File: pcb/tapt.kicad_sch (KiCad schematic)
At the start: 32 parts, among them J1 Conn_01x04_Pin, J2 Conn_01x04_MountingPin, SW1 SW_SPDT_XKB_DMx-xxxx-1, SW2 SW_SPST, U1 nRF52810-QCxx, Y1 32MHz

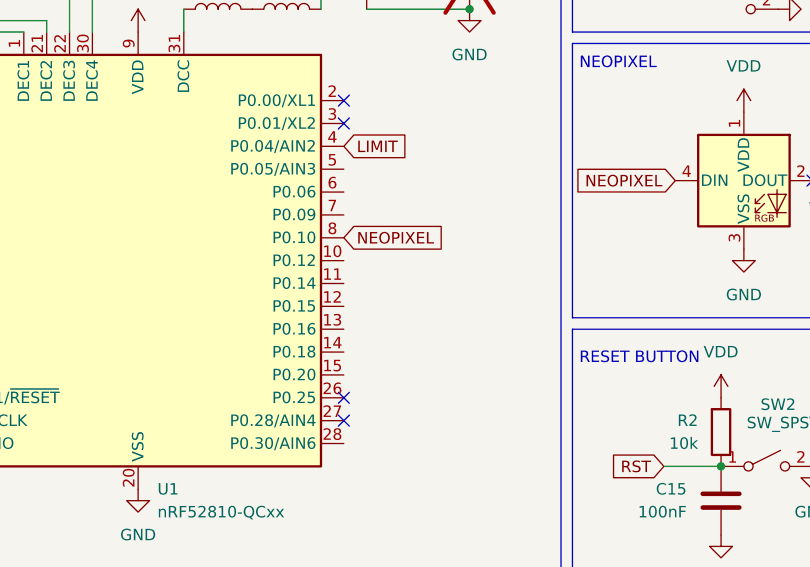
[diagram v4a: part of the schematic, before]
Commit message: pcb: uart, status led
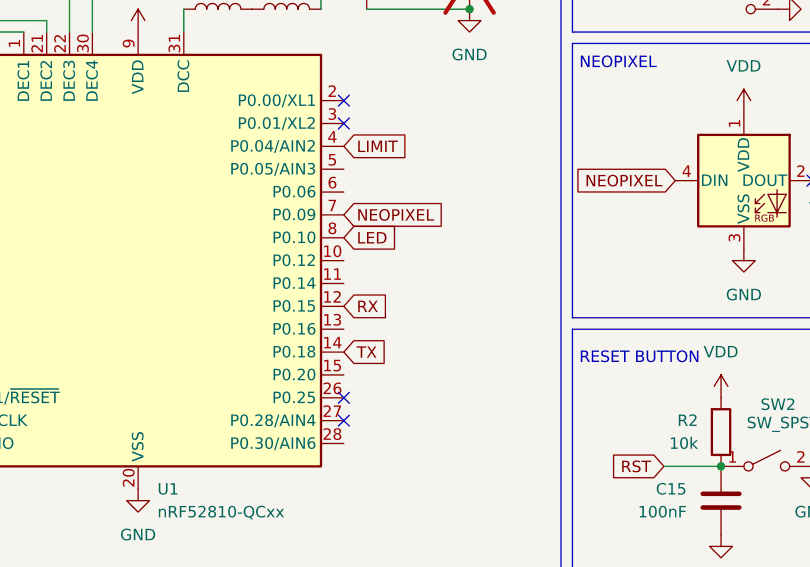
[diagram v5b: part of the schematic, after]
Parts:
- D2: LCSC (none) -> C2297
- J1, J2: now left out of the parts list
- R3: footprint Resistor_SMD:R_0805_2012Metric -> Resistor_SMD:R_0402_1005Metric; LCSC (none) -> C11702
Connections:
- net LED: now also U1.8 (P0.10)
- net NEOPIXEL: now also U1.7 (P0.09); no longer U1.8 (P0.10)
- net RX: now also U1.12 (P0.15)
- net TX: now also U1.14 (P0.18)
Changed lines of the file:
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@@
 		)
 	)
+	(global_label "NEOPIXEL"
+		(shape input)
+		(at 90.17 88.9 0)
+		(fields_autoplaced yes)
+		(effects
+			(font
+				(size 1.27 1.27)
+			)
+			(justify left)
+		)
+		(property "Intersheetrefs" "${INTERSHEET_REFS}"
+			(at 102.2266 88.9 0)
+			(effects
+				(font
+					(size 1.27 1.27)
+				)
+				(justify left)
+				(hide yes)
+			)
+		)
+	)
+	(global_label "RX"
+		(shape input)
+		(at 90.17 99.06 0)
+		(fields_autoplaced yes)
+		(effects
+			(font
+				(size 1.27 1.27)
+			)
+			(justify left)
+		)
+		(property "Intersheetrefs" "${INTERSHEET_REFS}"
+			(at 95.6347 99.06 0)
+			(effects
+				(font
+					(size 1.27 1.27)
+				)
+				(justify left)
+				(hide yes)
+			)
+		)
+	)
 	(global_label "SWDIO"
 		(shape input)
@@
 		)
 	)
+	(global_label "LED"
+		(shape input)
+		(at 90.17 91.44 0)
+		(fields_autoplaced yes)
+		(effects
+			(font
+				(size 1.27 1.27)
+			)
+			(justify left)
+		)
+		(property "Intersheetrefs" "${INTERSHEET_REFS}"
+			(at 96.6023 91.44 0)
+			(effects
+				(font
+					(size 1.27 1.27)
+				)
+				(justify left)
+				(hide yes)
+			)
+		)
+	)
+	(global_label "TX"
+		(shape input)
+		(at 90.17 104.14 0)
+		(fields_autoplaced yes)
+		(effects
+			(font
+				(size 1.27 1.27)
+			)
+			(justify left)
+		)
+		(property "Intersheetrefs" "${INTERSHEET_REFS}"
+			(at 95.3323 104.14 0)
+			(effects
+				(font
+					(size 1.27 1.27)
+				)
+				(justify left)
+				(hide yes)
+			)
+		)
+	)
 	(global_label "SWDCLK"
 		(shape input)
@@
 		)
 	)
-	(global_label "NEOPIXEL"
-		(shape input)
-		(at 90.17 91.44 0)
-		(fields_autoplaced yes)
-		(effects
-			(font
-				(size 1.27 1.27)
-			)
-			(justify left)
-		)
-		(property "Intersheetrefs" "${INTERSHEET_REFS}"
-			(at 102.2266 91.44 0)
-			(effects
-				(font
-					(size 1.27 1.27)
-				)
-				(justify left)
-				(hide yes)
-			)
-		)
-	)
 	(global_label "LED"
 		(shape input)
@@
 			)
 		)
+		(property "LCSC" "C2297"
+			(at 182.88 85.09 0)
+			(effects
+				(font
+					(size 1.27 1.27)
+				)
+				(hide yes)
+			)
+		)
 		(pin "2"
 		)
@@
 			)
 		)
-		(property "Footprint" "Resistor_SMD:R_0805_2012Metric"
+		(property "Footprint" "Resistor_SMD:R_0402_1005Metric"
 			(at 190.5 86.868 90)
 			(effects
@@
 			)
 		)
+		(property "LCSC" "C11702"
+			(at 190.5 85.09 90)
+			(effects
+				(font
+					(size 1.27 1.27)
+				)
+				(hide yes)
+			)
+		)
 		(pin "1"
 		)
@@
 		(unit 1)
 		(exclude_from_sim no)
-		(in_bom yes)
+		(in_bom no)
 		(on_board yes)
 		(dnp no)
@@
 		(unit 1)
 		(exclude_from_sim no)
-		(in_bom yes)
+		(in_bom no)
 		(on_board yes)
 		(dnp no)

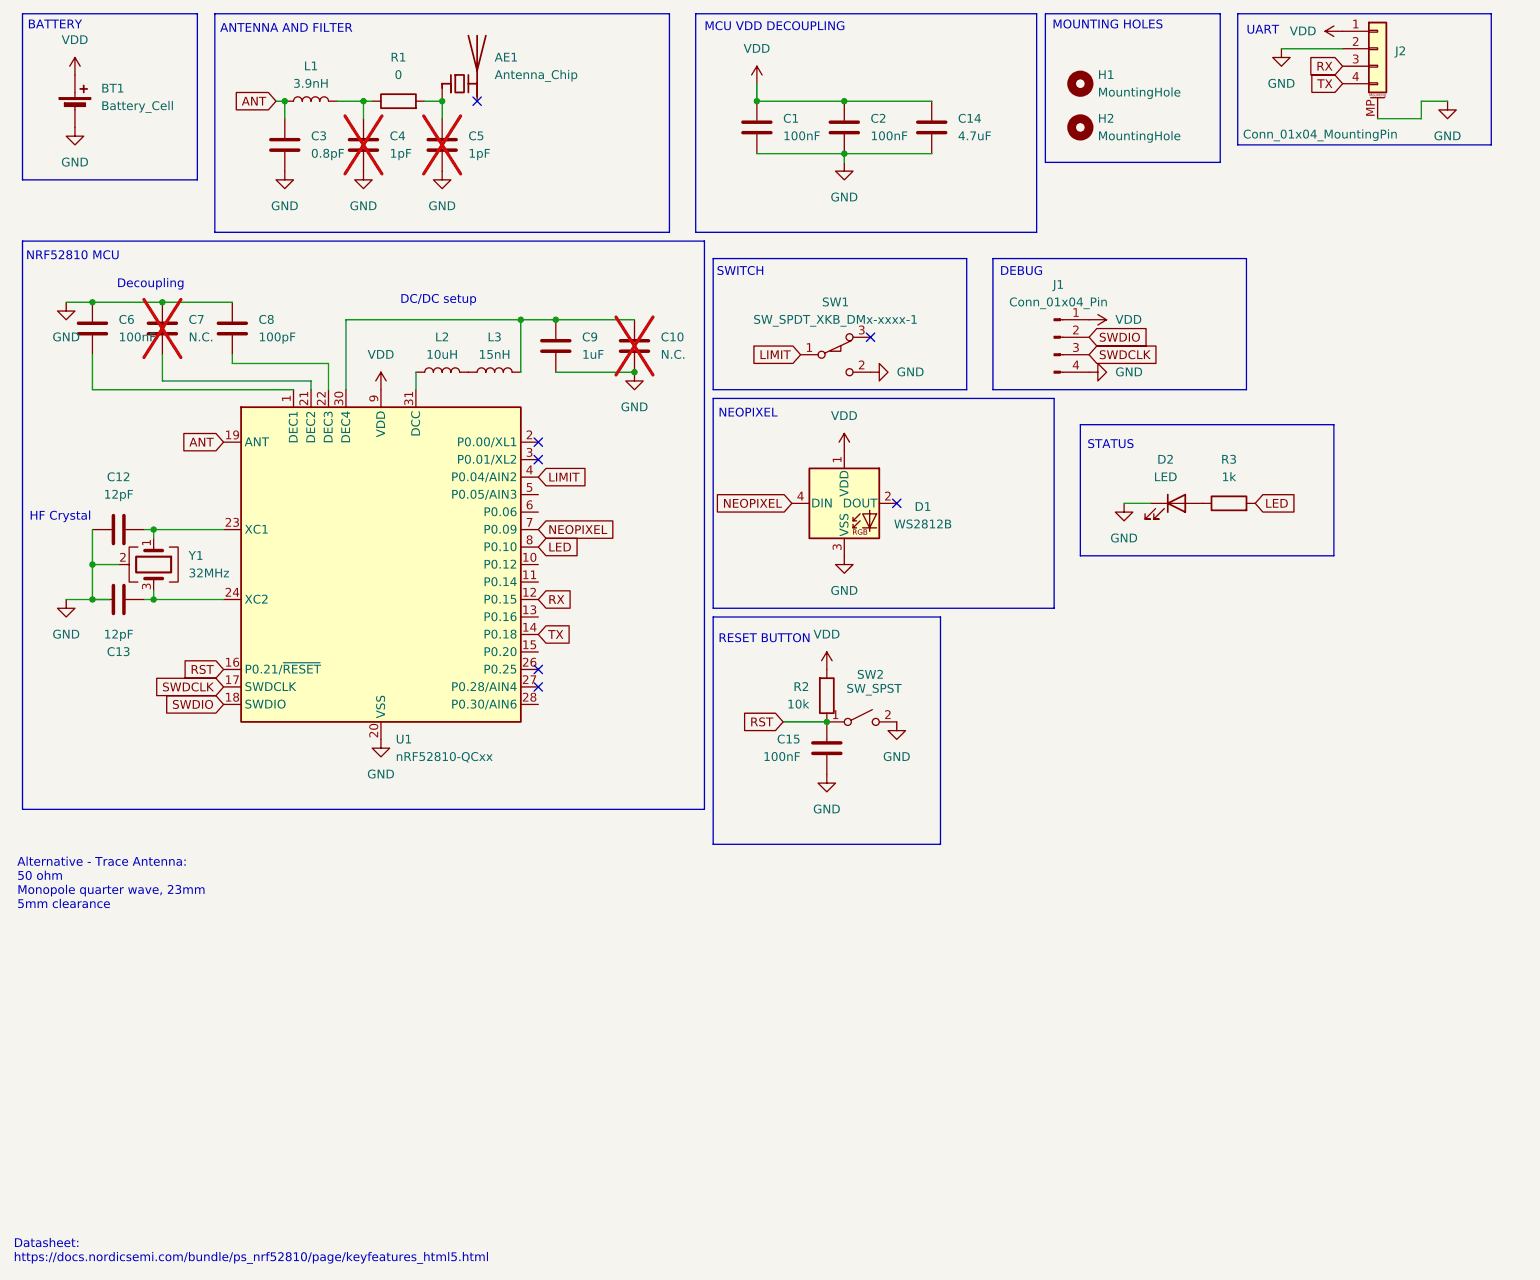
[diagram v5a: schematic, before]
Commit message: pcb: 4 layer redesign, more antenna tuning, low freq crystal
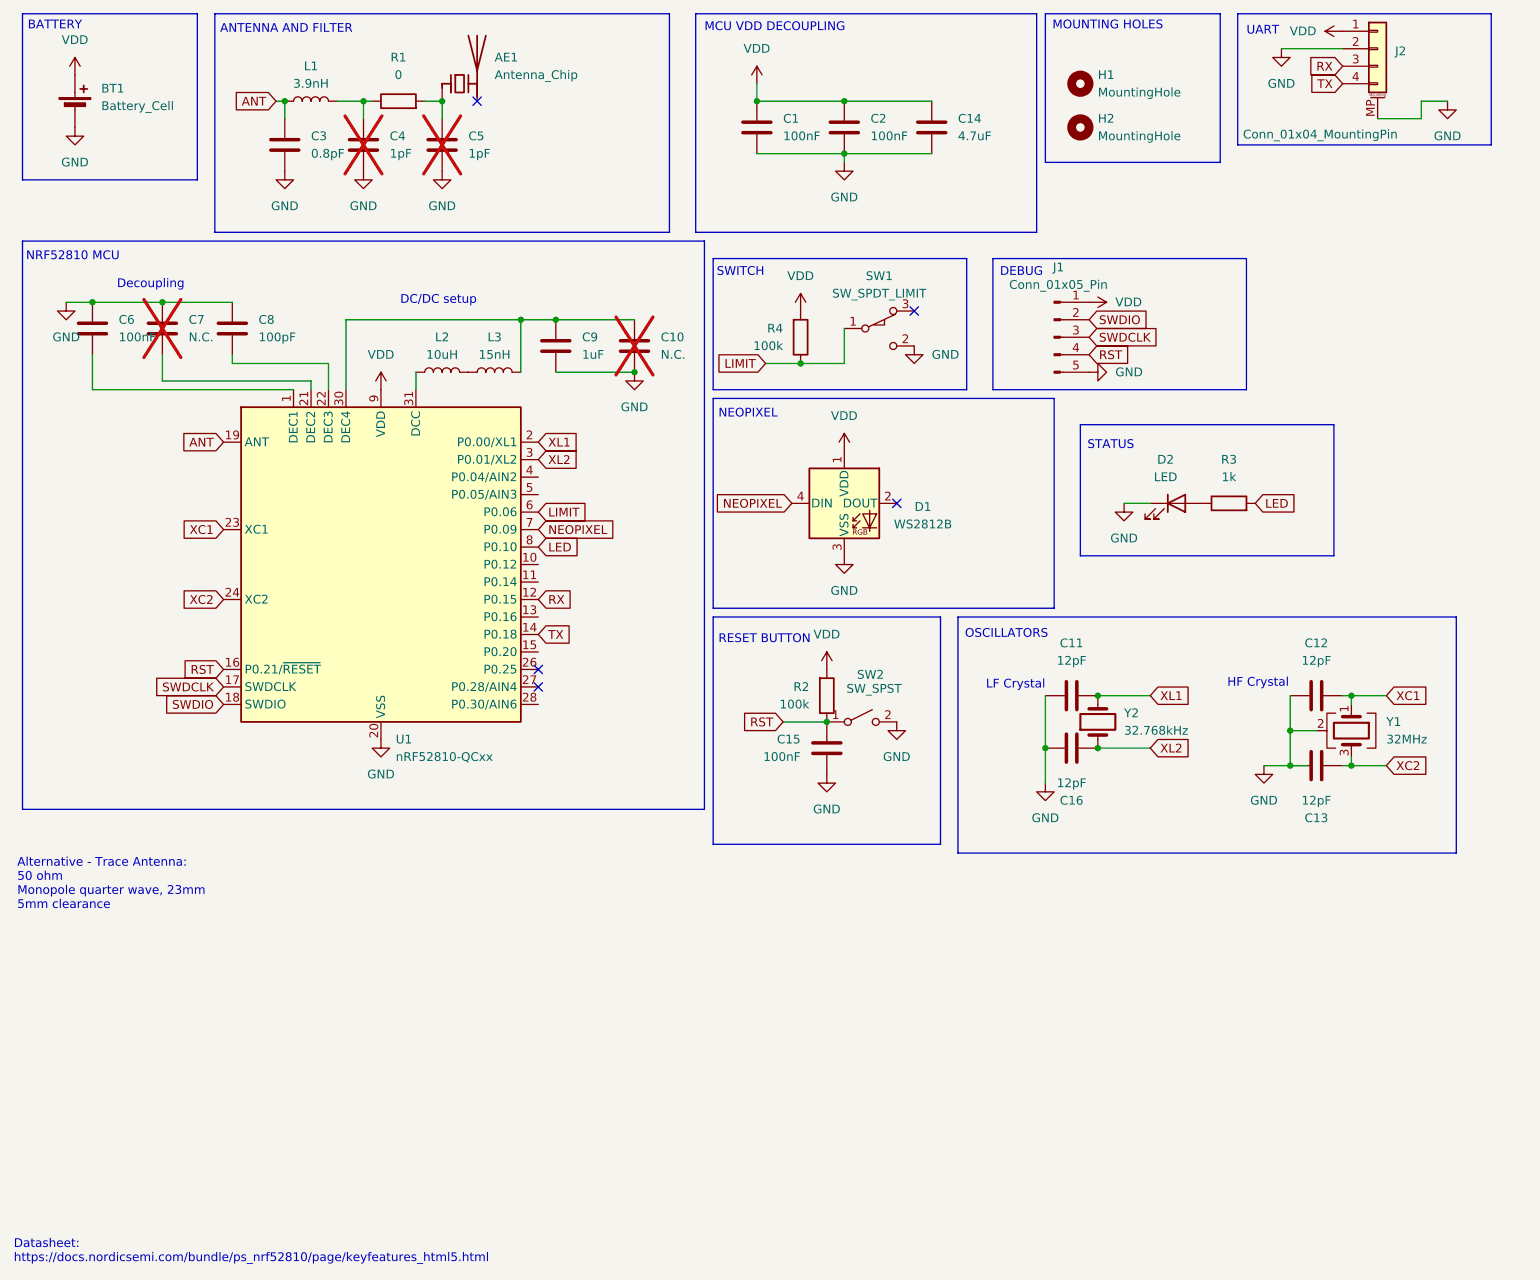
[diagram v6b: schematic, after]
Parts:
- added C11, C16: 12pF, Capacitor_SMD:C_0402_1005Metric, symbol Device:C
- added R4: 100k, Resistor_SMD:R_0402_1005Metric, symbol Device:R
- added Y2: 32.768kHz, Crystal:Crystal_SMD_2012-2Pin_2.0x1.2mm, symbol Device:Crystal
- J1: value Conn_01x04_Pin -> Conn_01x05_Pin; footprint Connector_PinHeader_2.54mm:PinHeader_1x04_P2.54mm_Vertical -> Connector_PinHeader_2.54mm:PinHeader_1x05_P2.54mm_Vertical; symbol Connector:Conn_01x04_Pin -> Connector:Conn_01x05_Pin; now in the parts list
- R2: value 10k -> 100k; LCSC C25744 -> C25741
- SW1: value SW_SPDT_XKB_DMx-xxxx-1 -> SW_SPDT_LIMIT
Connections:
- net GND: now also J1.5 (Pin_5), C11.1, C16.1; no longer J1.4 (Pin_4)
- net LIMIT: now also U1.6 (P0.06), R4.1; no longer U1.4 (P0.04/AIN2)
- net RST: now also J1.4 (Pin_4)
- net VDD: now also R4.2
- net XC1: now reaches C12.2, U1.23 (XC1), Y1.1
- net XC2: now reaches C13.2, U1.24 (XC2), Y1.3
- net XL1: now reaches U1.2 (P0.00/XL1)
- net XL1: now also C11.2, Y2.2
- net XL2: now reaches U1.3 (P0.01/XL2)
- net XL2: now also C16.2, Y2.1
- no-connect marks 7 -> 5
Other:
- note added: "LF Crystal"
- note added: "OSCILLATORS"
- moved on the sheet: C12, C13, SW1, Y1

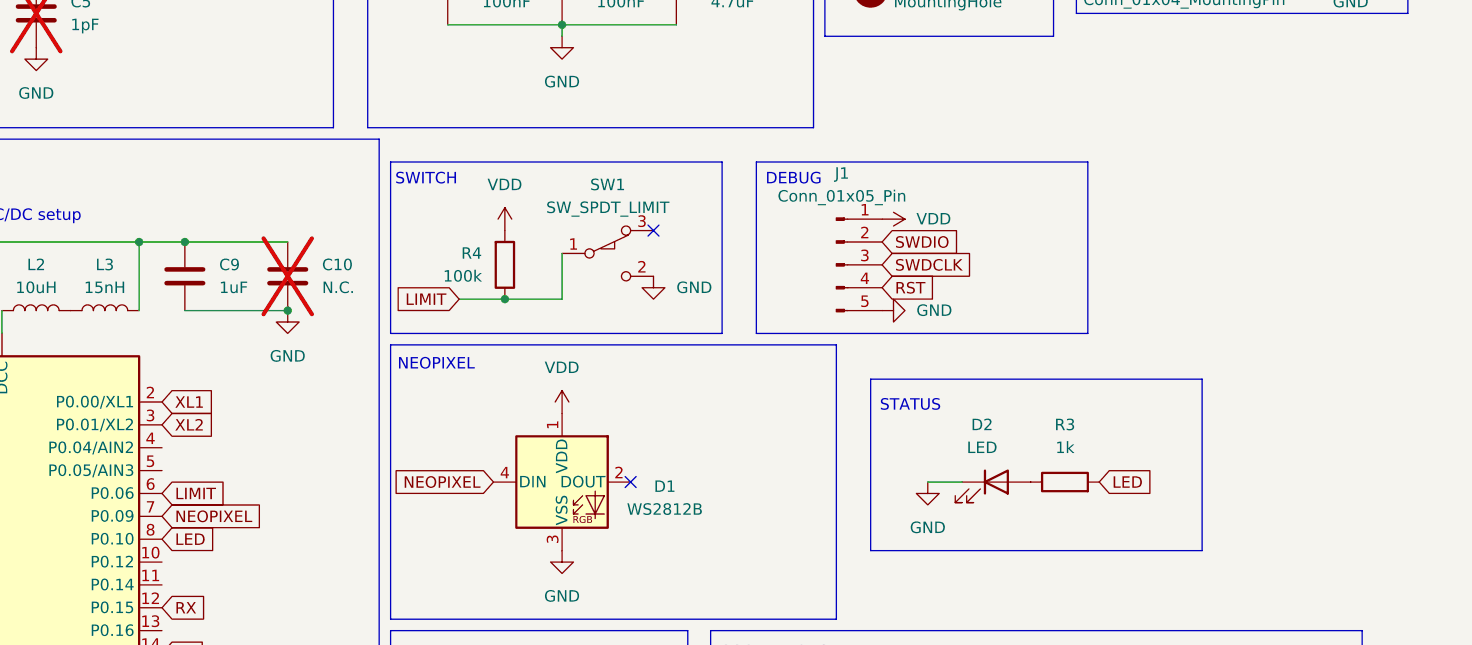
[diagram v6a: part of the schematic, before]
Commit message: pcb: battery voltagef divider, hf clock routing
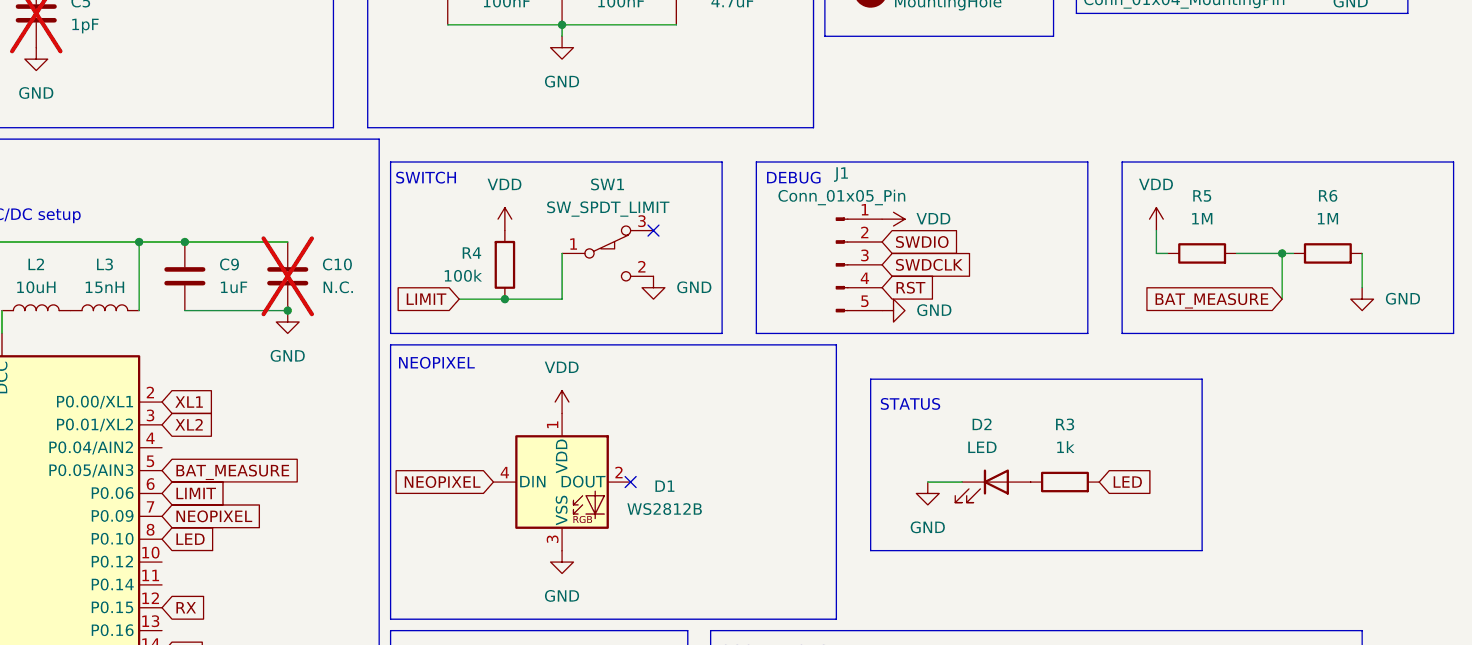
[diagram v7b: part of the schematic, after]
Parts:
- added R5, R6: 1M, Resistor_SMD:R_0402_1005Metric, symbol Device:R
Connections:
- net GND: now also R6.2
- net VDD: now also R5.1
- net BAT_MEASURE: now reaches U1.5 (P0.05/AIN3)
- net BAT_MEASURE: now also R5.2, R6.1
